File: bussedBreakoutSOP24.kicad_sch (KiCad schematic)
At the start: 51 parts, among them J1 Conn_01x12_Pin, J10 Conn_01x06_Pin, J11 Conn_01x06_Pin, J12 Conn_01x06_Pin, J13 Conn_01x06_Pin, J14 Conn_01x06_Pin, J15 Conn_01x06_Pin, J16 Conn_01x06_Pin, J17 Conn_01x06_Pin, J18 Conn_01x06_Pin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

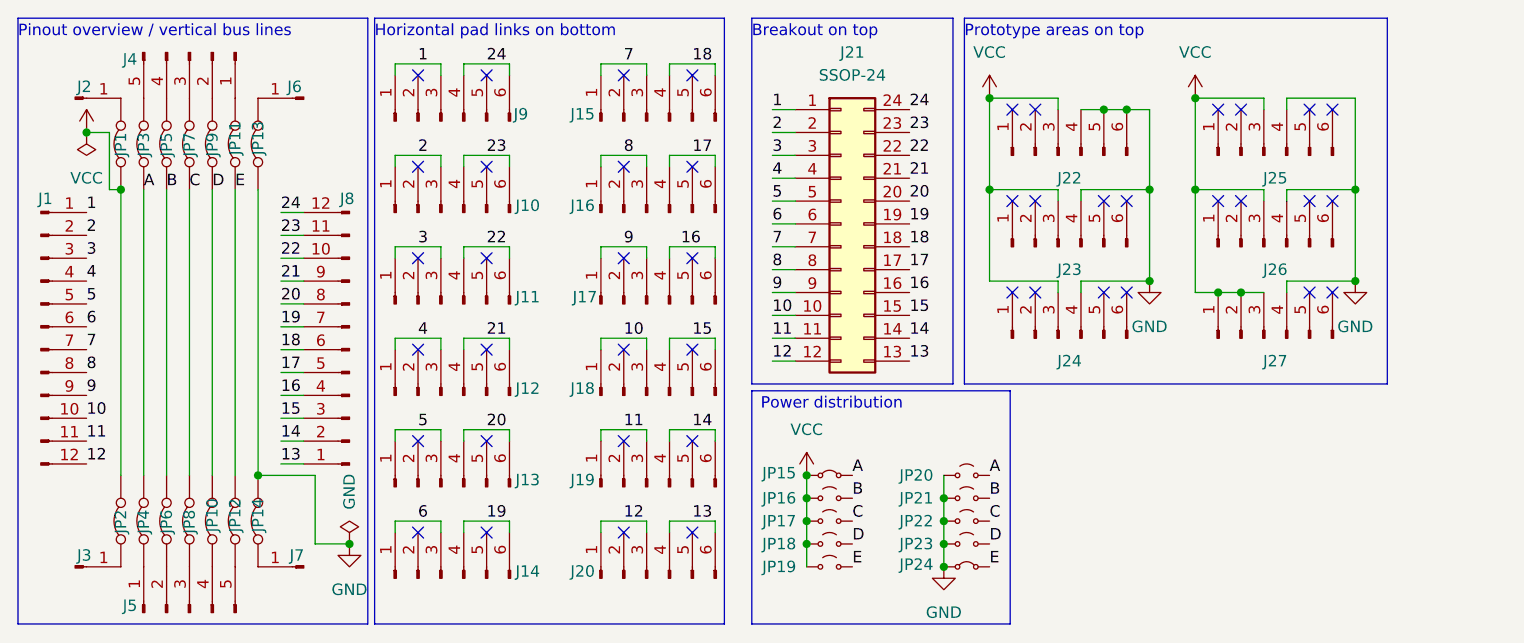
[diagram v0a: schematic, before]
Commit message: Change to a SOP24 breakout
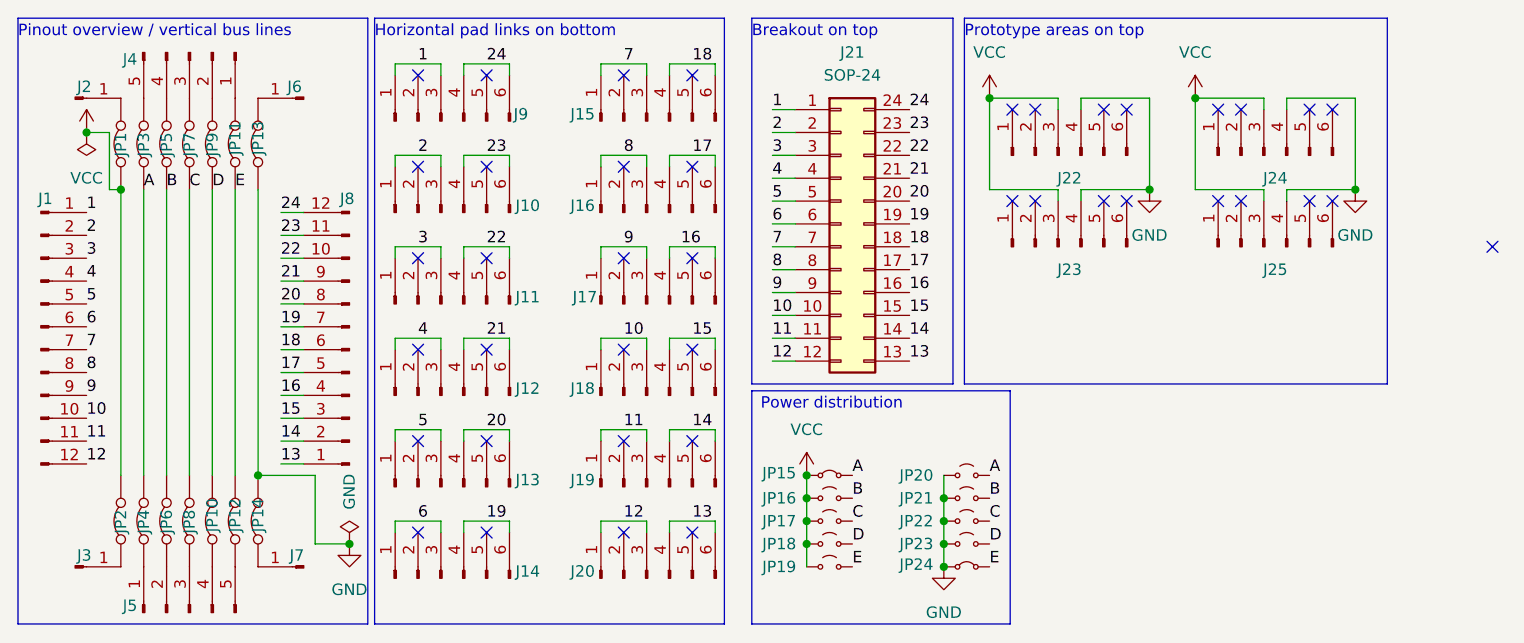
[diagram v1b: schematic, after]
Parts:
- removed J24, J27: Conn_01x06_Pin, SMD:SMD_0805_grid_1x6, symbol Connector:Conn_01x06_Pin
- J21: value SSOP-24 -> SOP-24; footprint SMD:SSOP-24_3.9-7.5mmx8.2mm_P0.65mm -> SMD:SOP-24_3.9-7.5mmx15.4mm_P1.27mm
- renumbered J25 to J24, J26 to J25
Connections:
- net GND: no longer J22.5 (Pin_5), J22.6 (Pin_6)
- no-connect marks 44 -> 41

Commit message: Change prototype area 0402s and connect it to VCC+GND+middle rows of pads on bottom
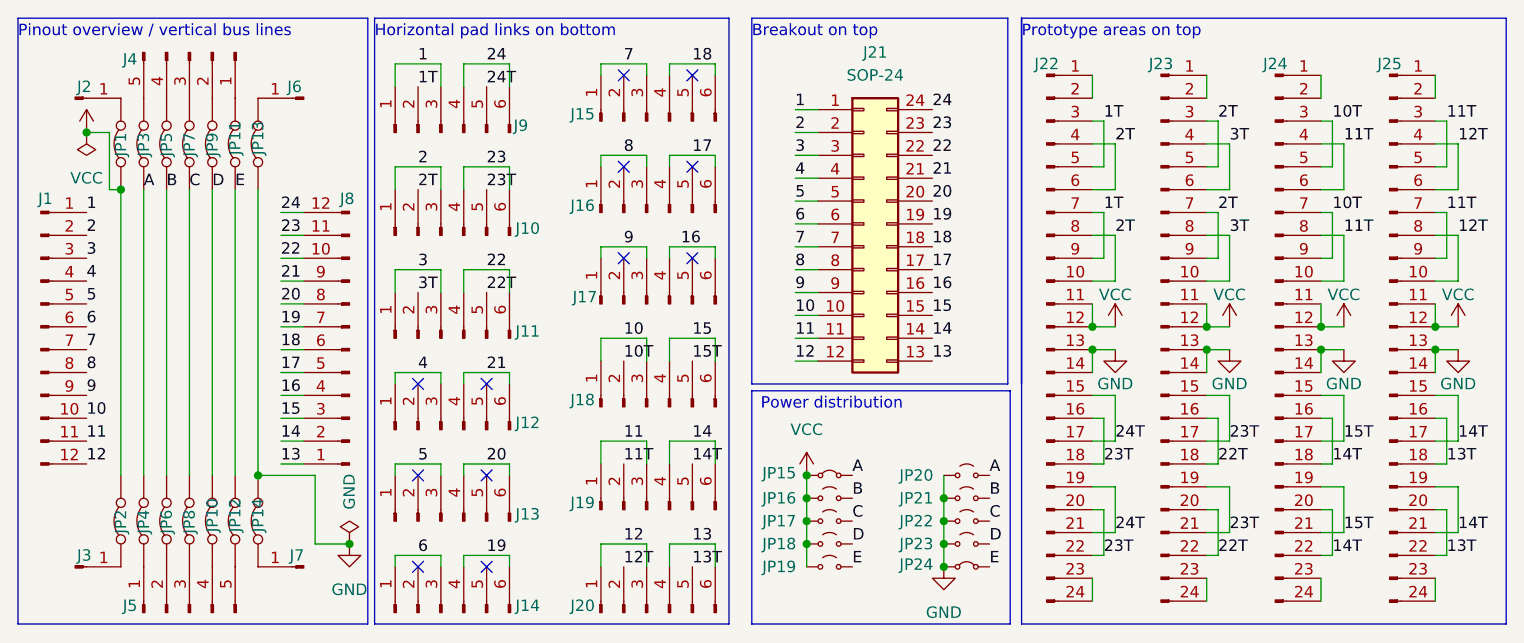
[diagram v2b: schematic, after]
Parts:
- removed J22, J23, J24, J25: Conn_01x06_Pin, SMD:SMD_0805_grid_1x6, symbol Connector:Conn_01x06_Pin
- added J22, J23, J24, J25: Conn_01x24_Pin, SMD:SMD_grid_2x12_0402, symbol Connector:Conn_01x24_Pin
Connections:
- net GND: now also J22.13 (Pin_13), J22.14 (Pin_14), J23.13 (Pin_13), J23.14 (Pin_14), J24.13 (Pin_13), J24.14 (Pin_14), J25.13 (Pin_13), J25.14 (Pin_14)
- net VCC: now also J22.11 (Pin_11), J22.12 (Pin_12), J23.11 (Pin_11), J23.12 (Pin_12), J24.11 (Pin_11), J24.12 (Pin_12), J25.11 (Pin_11), J25.12 (Pin_12)
- net 11T: now reaches J19.2 (Pin_2)
- net 11T: now also J24.10 (Pin_10), J24.4 (Pin_4), J24.6 (Pin_6), J24.8 (Pin_8), J25.3 (Pin_3), J25.5 (Pin_5), J25.7 (Pin_7), J25.9 (Pin_9)
- net 14T: now reaches J19.5 (Pin_5)
- net 14T: now also J24.16 (Pin_16), J24.18 (Pin_18), J24.20 (Pin_20), J24.22 (Pin_22), J25.15 (Pin_15), J25.17 (Pin_17), J25.19 (Pin_19), J25.21 (Pin_21)
- net 2T: now reaches J10.2 (Pin_2)
- net 2T: now also J22.10 (Pin_10), J22.4 (Pin_4), J22.6 (Pin_6), J22.8 (Pin_8), J23.3 (Pin_3), J23.5 (Pin_5), J23.7 (Pin_7), J23.9 (Pin_9)
- net 23T: now reaches J10.5 (Pin_5)
- net 23T: now also J22.16 (Pin_16), J22.18 (Pin_18), J22.20 (Pin_20), J22.22 (Pin_22), J23.15 (Pin_15), J23.17 (Pin_17), J23.19 (Pin_19), J23.21 (Pin_21)
- net 10T: now reaches J18.2 (Pin_2)
- net 10T: now also J24.3 (Pin_3), J24.5 (Pin_5), J24.7 (Pin_7), J24.9 (Pin_9)
- net 15T: now reaches J18.5 (Pin_5)
- net 15T: now also J24.15 (Pin_15), J24.17 (Pin_17), J24.19 (Pin_19), J24.21 (Pin_21)
- net 3T: now reaches J11.2 (Pin_2)
- net 3T: now also J23.10 (Pin_10), J23.4 (Pin_4), J23.6 (Pin_6), J23.8 (Pin_8)
- net 22T: now reaches J11.5 (Pin_5)
- net 22T: now also J23.16 (Pin_16), J23.18 (Pin_18), J23.20 (Pin_20), J23.22 (Pin_22)
- net 1T: now reaches J9.2 (Pin_2)
- net 1T: now also J22.3 (Pin_3), J22.5 (Pin_5), J22.7 (Pin_7), J22.9 (Pin_9)
- net 24T: now reaches J9.5 (Pin_5)
- net 24T: now also J22.15 (Pin_15), J22.17 (Pin_17), J22.19 (Pin_19), J22.21 (Pin_21)
- net 12T: now reaches J20.2 (Pin_2)
- net 12T: now also J25.10 (Pin_10), J25.4 (Pin_4), J25.6 (Pin_6), J25.8 (Pin_8)
- net 13T: now reaches J20.5 (Pin_5)
- net 13T: now also J25.16 (Pin_16), J25.18 (Pin_18), J25.20 (Pin_20), J25.22 (Pin_22)
- new net: J24.1 (Pin_1), J24.2 (Pin_2)
- new net: J24.23 (Pin_23), J24.24 (Pin_24)
- new net: J25.1 (Pin_1), J25.2 (Pin_2)
- new net: J25.23 (Pin_23), J25.24 (Pin_24)
- new net: J22.1 (Pin_1), J22.2 (Pin_2)
- new net: J22.23 (Pin_23), J22.24 (Pin_24)
- new net: J23.1 (Pin_1), J23.2 (Pin_2)
- new net: J23.23 (Pin_23), J23.24 (Pin_24)
- no-connect marks 41 -> 12
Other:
- moved on the sheet: J10, J11, J12, J13, J14, J18, J19, J20, J21, J9

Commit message: Fix/exclude DRC errors
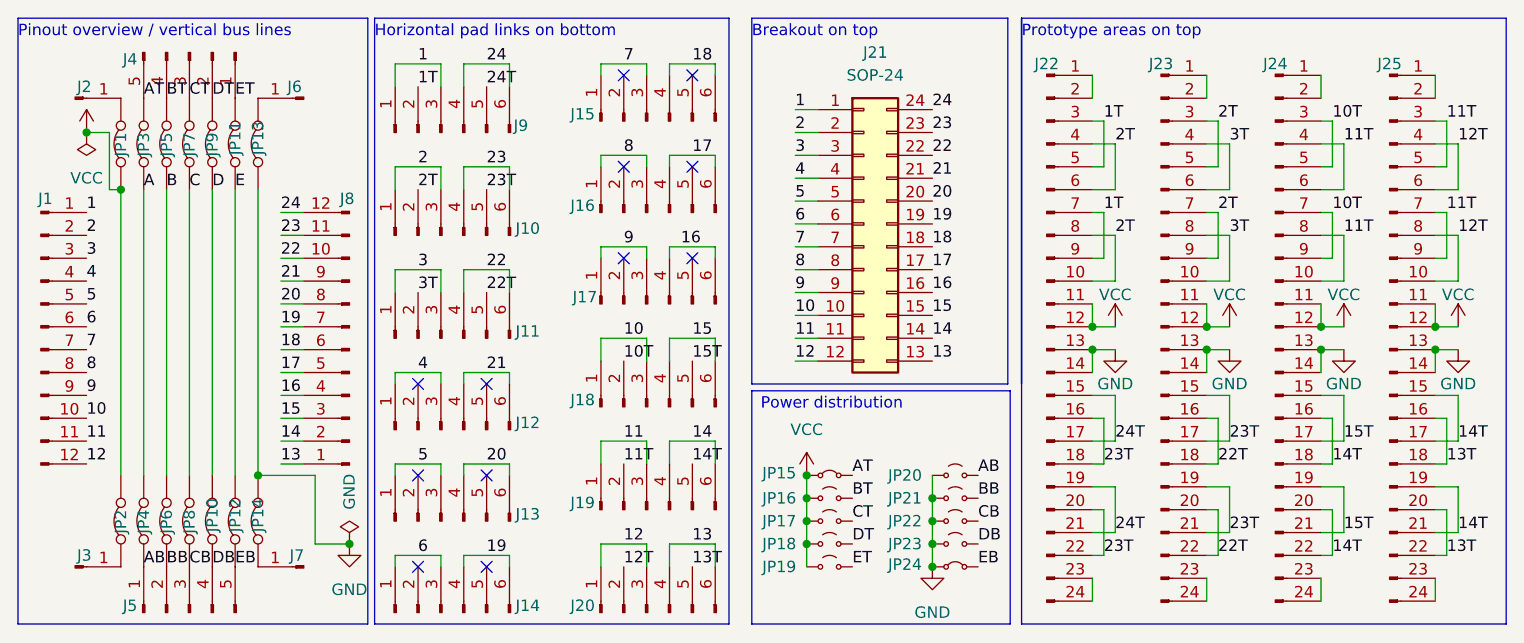
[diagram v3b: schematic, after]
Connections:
- net A: no longer JP15.2 (B), JP20.2 (B)
- net B: no longer JP16.2 (B), JP21.2 (B)
- net C: no longer JP17.2 (B), JP22.2 (B)
- net D: no longer JP18.2 (B), JP23.2 (B)
- net E: no longer JP19.2 (B), JP24.2 (B)
- net BB: now reaches J5.2 (Pin_2), JP6.1 (A)
- net BB: now also JP21.2 (B)
- net BT: now reaches J4.4 (Pin_4), JP5.2 (B)
- net BT: now also JP16.2 (B)
- net AB: now reaches J5.1 (Pin_1), JP4.1 (A)
- net AB: now also JP20.2 (B)
- net CB: now reaches J5.3 (Pin_3), JP8.1 (A)
- net CB: now also JP22.2 (B)
- net DB: now reaches J5.4 (Pin_4), JP10.1 (A)
- net DB: now also JP23.2 (B)
- net EB: now reaches J5.5 (Pin_5), JP12.1 (A)
- net EB: now also JP24.2 (B)
- net ET: now reaches J4.1 (Pin_1), JP11.2 (B)
- net ET: now also JP19.2 (B)
- net DT: now reaches J4.2 (Pin_2), JP9.2 (B)
- net DT: now also JP18.2 (B)
- net CT: now reaches J4.3 (Pin_3), JP7.2 (B)
- net CT: now also JP17.2 (B)
- net AT: now reaches J4.5 (Pin_5), JP3.2 (B)
- net AT: now also JP15.2 (B)
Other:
- moved on the sheet: JP20, JP21, JP22, JP23, JP24
